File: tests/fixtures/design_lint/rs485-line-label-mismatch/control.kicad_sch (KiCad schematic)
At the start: 1 part, among them U1 RS-485 transceiver

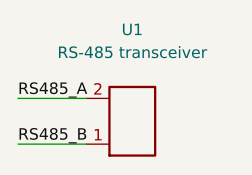
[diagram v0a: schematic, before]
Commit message: Correct RS-485 native fixture pin assignments
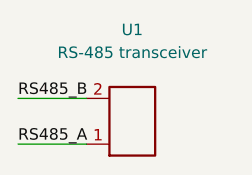
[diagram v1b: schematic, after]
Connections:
- net RS485_A: now also U1.1 (A); no longer U1.2 (B)
- net RS485_B: now also U1.2 (B); no longer U1.1 (A)
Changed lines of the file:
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@@
   (wire (pts (xy 58.42 60.96) (xy 50.80 60.96))
     (stroke (width 0) (type default)))
-  (label "RS485_A" (at 50.80 60.96 0)
+  (label "RS485_B" (at 50.80 60.96 0)
     (effects (font (size 1.27 1.27)) (justify left bottom))
 )
   (wire (pts (xy 58.42 66.04) (xy 50.80 66.04))
     (stroke (width 0) (type default)))
-  (label "RS485_B" (at 50.80 66.04 0)
+  (label "RS485_A" (at 50.80 66.04 0)
     (effects (font (size 1.27 1.27)) (justify left bottom))
 )
